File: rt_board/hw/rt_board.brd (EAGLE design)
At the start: 100 x 80 mm, 26 parts, among them IC1 MCP170333MB, Q1 8MHz, U1 STM32F051R8T7, U2 SN74AVC4T245PW, X1 PWR

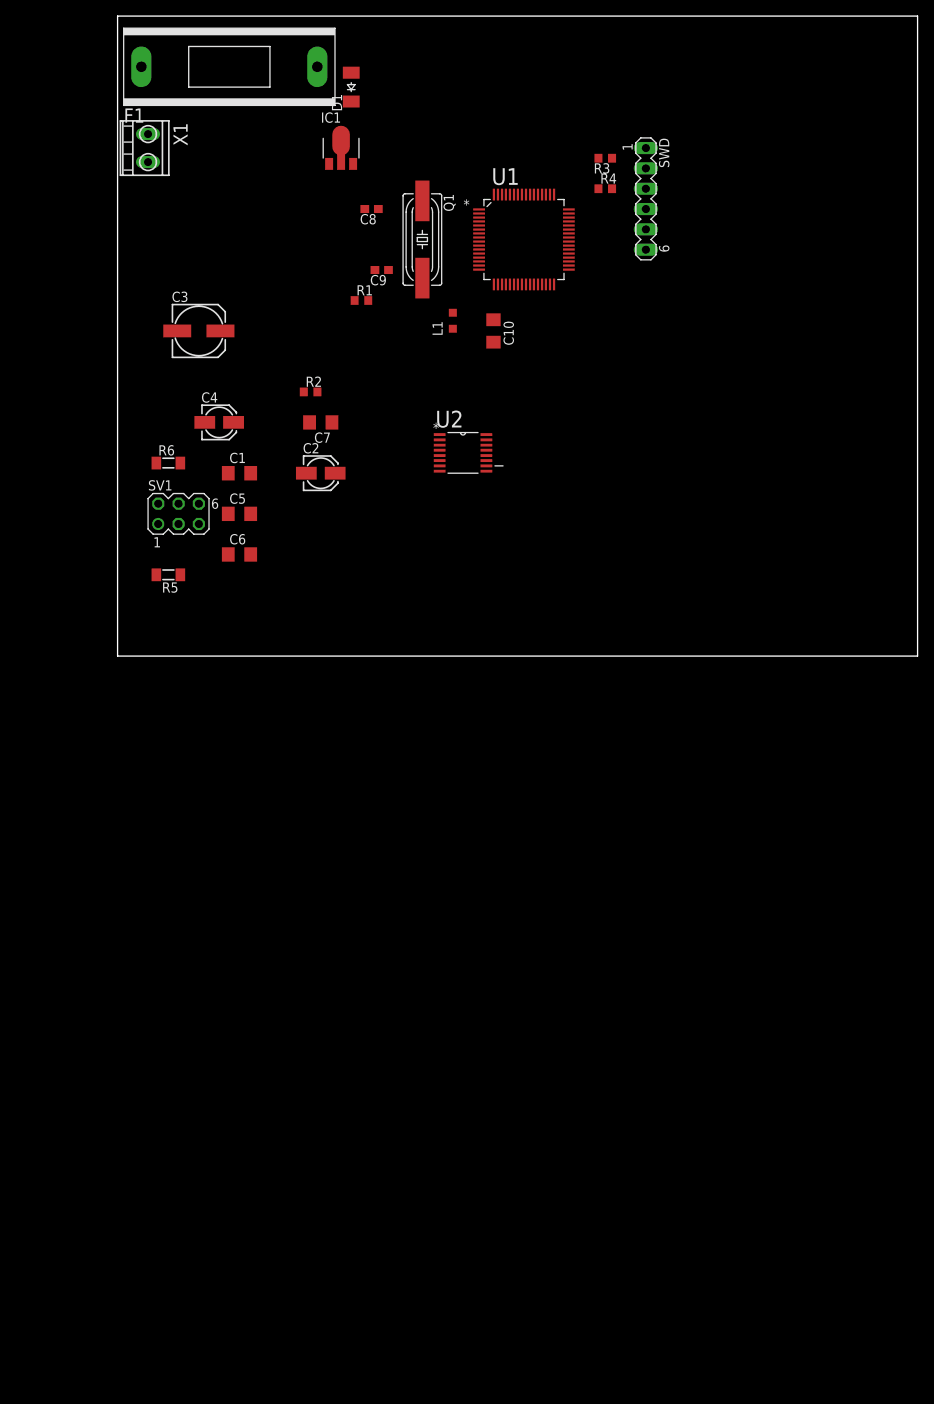
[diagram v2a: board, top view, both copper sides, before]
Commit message: added power outputs and current control circutyr
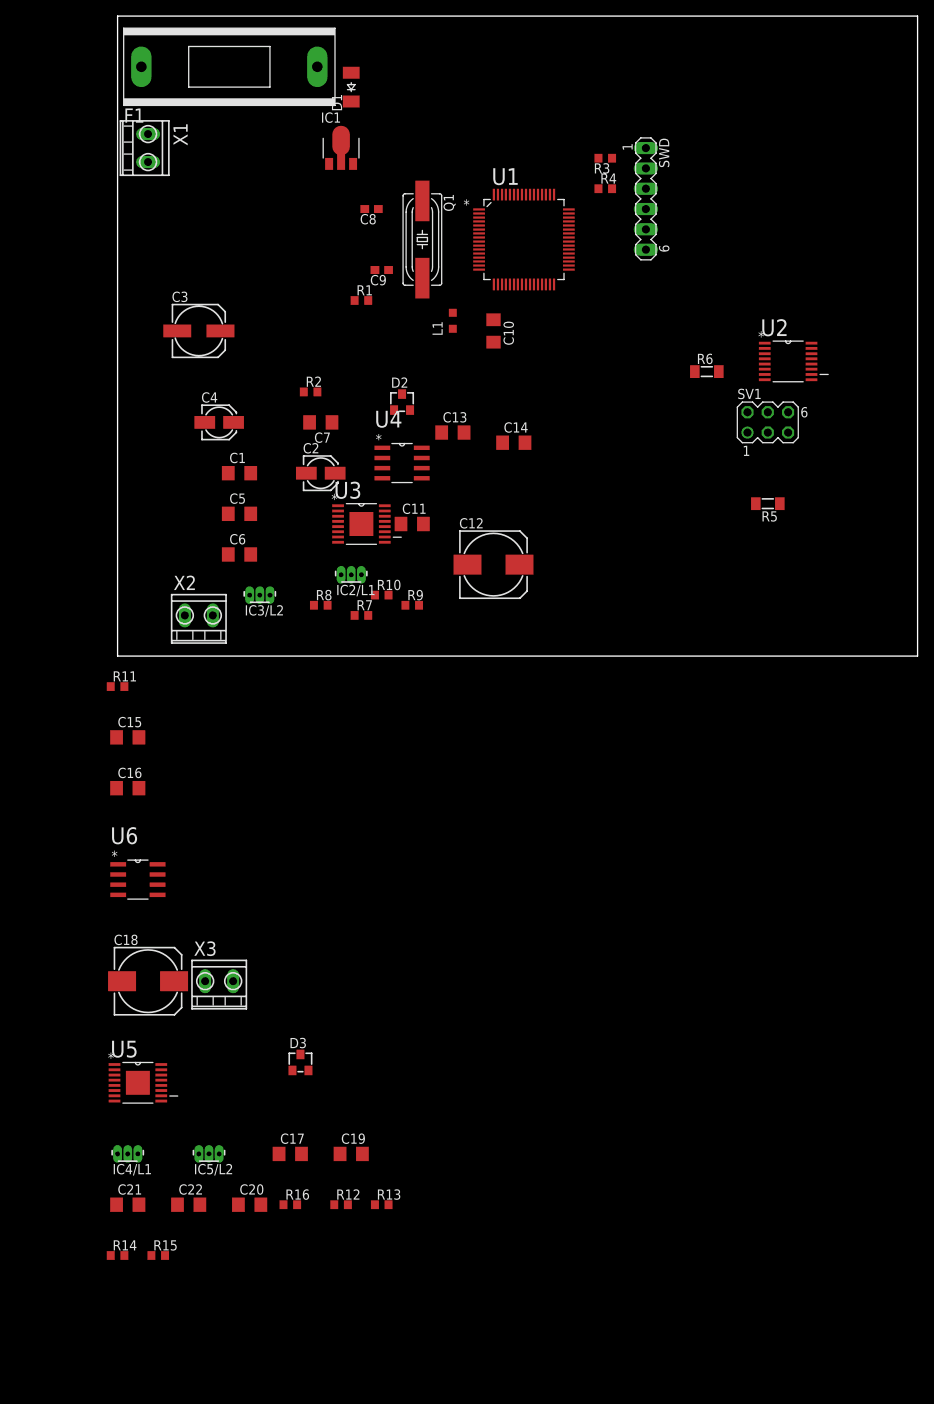
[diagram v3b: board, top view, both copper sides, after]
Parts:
- added C11, C13, C15, C16, C17, C19, C21, C22: 100nF, rcl:C1206
- added C12, C18: 100uF, rcl:153CLV-0810
- added C14, C20: 1nF, rcl:C1206
- added D2, D3: BZX84CSMD, diode:TO236
- added IC2/L1, IC3/L2, IC4/L1, IC5/L2: TLE4935L, allegro:SIP3-UA
- added R10, R13, R15, R8: 3kR, rcl:R0603
- added R11, R16: 3.3kR, rcl:R0603
- added R12, R14, R7, R9: 2kR, rcl:R0603
- added U3, U5: DRV8801PWP, TI-DRV8801PWP:SOP65P640X120-17N
- added U4, U6: ACS712ELCTR-20A-T, Allegro-ACS712ELCTR-20A-T:SOIC127P600X175-8N
- added X2: LEFT, con-ptr500:AK550/2
- added X3: RIGHT, con-ptr500:AK550/2
- moved R5 75.5 mm to (81.3, 19.1)
- moved SV1 74.5 mm to (81.3, 29.2)
- moved R6 68.3 mm to (73.7, 35.6)
- moved U2 42.2 mm to (83.8, 36.8)
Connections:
- new net N$16: IC2/L1.3, R7.1
- new net N$17: R7.2, R8.1, U1.14
- new net N$18: IC3/L2.3, R9.1
- new net N$19: R10.1, R9.2, U1.15
- new net N$20: U3.7, X2.1
- new net N$21: U3.10, X2.2
- new net N$22: U3.8, U4.1, U4.2
- new net N$23: D2.C, U1.20, U4.7
- new net N$24: C14.1, U4.6
- new net N$25: R11.1, U3.5
- new net N$26: C15.2, U3.14
- new net N$27: C16.2, U3.12
- new net N$28: C16.1, U3.11
- new net N$29: IC4/L1.3, R12.1
- new net N$30: R12.2, R13.1, U1.56
- new net N$31: IC5/L2.3, R14.1
- new net N$32: R14.2, R15.1, U1.57
- new net N$33: U5.7, X3.1
- new net N$34: U5.10, X3.2
- new net N$35: C20.1, U6.6
- new net N$36: U5.8, U6.1, U6.2
- new net N$37: D3.C, U1.21, U6.7
- new net N$38: R16.1, U5.5
- new net N$39: C21.2, U5.14
- new net N$40: C22.2, U5.12
- new net N$41: C22.1, U5.11
- new net N$42: U1.34, U3.2, U5.2
- new net N$45: U1.35, U3.6
- new net N$46: U1.36, U5.6
- new net N$48: U1.33, U3.3
- new net N$49: U1.30, U5.3
- net +12V: now also C11.1, C12.+, C15.1, C17.1, C18.+, C21.1, U3.9, U5.9
- net +5V/1: now also C13.1, C19.1, IC2/L1.1, IC3/L2.1, IC4/L1.1, IC5/L2.1, U4.8, U6.8
- net +5V/4: now also R11.2, R16.2
- net 0V: now also C11.2, C12.-, C13.2, C14.2, C17.2, C18.-, C19.2, C20.2, D2.A, D3.A, IC2/L1.2, IC3/L2.2, IC4/L1.2, IC5/L2.2, R10.2, R13.2, R15.2, R8.2, U3.13, U3.16, U3.17, U3.4, U4.3, U4.4, U4.5, U5.13, U5.16, U5.17, U5.4, U6.3, U6.4, U6.5

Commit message: added LED to indicate circut is powered and one user-defined, controlled via uC
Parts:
- added LED1, LED2: GREEN, led:CHIPLED_0603
- added R17: 470R, rcl:R0603
- added U7: 2N7002BKW, 2n7002:SOT65P210X110-3N
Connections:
- new net N$43: LED1.A, R17.2
- new net N$44: U1.26, U7.1
- new net N$47: LED2.C, U7.3
- net +5V: now also LED2.A, R17.1
- net 0V: now also LED1.C, U7.2
- net N$17: now also U1.41; no longer U1.14
- net N$19: now also U1.42; no longer U1.15
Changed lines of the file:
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@@
 <element name="C21" library="rcl" package="C1206" value="100nF" x="1.27" y="-68.58"/>
 <element name="C22" library="rcl" package="C1206" value="100nF" x="8.89" y="-68.58"/>
+<element name="LED1" library="led" package="CHIPLED_0603" value="GREEN" x="-5.08" y="-74.93"/>
+<element name="R17" library="rcl" package="R0603" value="470R" x="-5.08" y="-80.01"/>
+<element name="U7" library="2n7002" package="SOT65P210X110-3N" value="2N7002BKW" x="-2.54" y="-87.63">
+<attribute name="PACKAGE" value="SOT-3" x="-2.54" y="-87.63" size="1.778" layer="27" display="off"/>
+<attribute name="OC_NEWARK" value="55T7739" x="-2.54" y="-87.63" size="1.778" layer="27" display="off"/>
+<attribute name="MPN" value="2N7002BKW" x="-2.54" y="-87.63" size="1.778" layer="27" display="off"/>
+<attribute name="SUPPLIER" value="NXP Semiconductors" x="-2.54" y="-87.63" size="1.778" layer="27" display="off"/>
+<attribute name="OC_FARNELL" value="1894713" x="-2.54" y="-87.63" size="1.778" layer="27" display="off"/>
+</element>
+<element name="LED2" library="led" package="CHIPLED_0603" value="GREEN" x="-10.16" y="-90.17"/>
 </elements>
 <signals>
@@
 <contactref element="U3" pad="16"/>
 <contactref element="U5" pad="16"/>
+<contactref element="LED1" pad="C"/>
+<contactref element="U7" pad="2"/>
 <wire x1="61.81" y1="62.23" x2="66.04" y2="58.42" width="0" layer="19" extent="1-1"/>
 <wire x1="47.5488" y1="57.6834" x2="61.81" y2="62.23" width="0" layer="19" extent="1-1"/>
@@
 <wire x1="33.87" y1="-68.58" x2="30.61" y2="-62.23" width="0" layer="19" extent="1-1"/>
 <wire x1="21.86" y1="-51.8" x2="22.99" y2="-62.23" width="0" layer="19" extent="1-1"/>
-<wire x1="5.93" y1="-74.93" x2="1.27" y2="-62.23" width="0" layer="19" extent="1-1"/>
+<wire x1="-5.08" y1="-74.18" x2="1.27" y2="-62.23" width="0" layer="19" extent="1-1"/>
+<wire x1="5.93" y1="-74.93" x2="-5.08" y2="-74.18" width="0" layer="19" extent="1-1"/>
+<wire x1="-3.4798" y1="-88.2904" x2="-5.08" y2="-74.18" width="0" layer="19" extent="1-1"/>
 </signal>
 <signal name="+5V">
@@
 <contactref element="R4" pad="2"/>
 <contactref element="U2" pad="16"/>
+<contactref element="R17" pad="1"/>
+<contactref element="LED2" pad="A"/>
 <wire x1="61.81" y1="58.42" x2="66.04" y2="63.5" width="0" layer="19" extent="1-1"/>
 <wire x1="54.5592" y1="46.4566" x2="61.81" y2="58.42" width="0" layer="19" extent="1-1"/>
@@
 <wire x1="41.91" y1="40.91" x2="54.5592" y2="46.4566" width="0" layer="19" extent="1-1"/>
 <wire x1="29.439" y1="61.519" x2="45.1866" y2="55.8292" width="0" layer="19" extent="1-1"/>
-<wire x1="86.741" y1="39.116" x2="41.91" y2="40.91" width="0" layer="19" extent="1-1"/>
 <wire x1="23.28" y1="33.02" x2="41.91" y2="40.91" width="0" layer="19" extent="1-1"/>
 <wire x1="14.5" y1="29.21" x2="23.28" y2="33.02" width="0" layer="19" extent="1-1"/>
@@
 <wire x1="13.84" y1="12.7" x2="13.84" y2="17.78" width="0" layer="19" extent="1-1"/>
 <wire x1="27.2" y1="22.86" x2="23.28" y2="33.02" width="0" layer="19" extent="1-1"/>
+<wire x1="86.741" y1="39.116" x2="61.81" y2="58.42" width="0" layer="19" extent="1-1"/>
+<wire x1="-5.93" y1="-80.01" x2="13.84" y2="12.7" width="0" layer="19" extent="1-1"/>
+<wire x1="-10.16" y1="-90.92" x2="-5.93" y2="-80.01" width="0" layer="19" extent="1-1"/>
 </signal>
 <signal name="+12V">
@@
 <contactref element="R7" pad="2"/>
 <contactref element="R8" pad="1"/>
-<contactref element="U1" pad="14"/>
-<wire x1="31.33" y1="5.08" x2="45.1866" y2="49.3268" width="0" layer="19" extent="1-1"/>
+<contactref element="U1" pad="41"/>
+<wire x1="31.33" y1="5.08" x2="56.4134" y2="52.324" width="0" layer="19" extent="1-1"/>
 <wire x1="24.55" y1="6.35" x2="31.33" y2="5.08" width="0" layer="19" extent="1-1"/>
 </signal>
@@
 <contactref element="R9" pad="2"/>
 <contactref element="R10" pad="1"/>
-<contactref element="U1" pad="15"/>
-<wire x1="37.68" y1="6.35" x2="45.1866" y2="48.8188" width="0" layer="19" extent="1-1"/>
+<contactref element="U1" pad="42"/>
+<wire x1="37.68" y1="6.35" x2="56.4134" y2="52.832" width="0" layer="19" extent="1-1"/>
 <wire x1="32.17" y1="7.62" x2="37.68" y2="6.35" width="0" layer="19" extent="1-1"/>
 </signal>
@@
 <wire x1="-0.381" y1="-52.3748" x2="53.5432" y2="46.4566" width="0" layer="19" extent="1-1"/>
 </signal>
+<signal name="N$43">
+<contactref element="LED1" pad="A"/>
+<contactref element="R17" pad="2"/>
+<wire x1="-5.08" y1="-75.68" x2="-4.23" y2="-80.01" width="0" layer="19" extent="1-1"/>
+</signal>
+<signal name="N$44">
+<contactref element="U1" pad="26"/>
+<contactref element="U7" pad="1"/>
+<wire x1="-3.4798" y1="-86.9696" x2="51.562" y2="46.4566" width="0" layer="19" extent="1-1"/>
+</signal>
+<signal name="N$47">
+<contactref element="U7" pad="3"/>
+<contactref element="LED2" pad="C"/>
+<wire x1="-1.6002" y1="-87.63" x2="-10.16" y2="-89.42" width="0" layer="19" extent="1-1"/>
+</signal>
 </signals>

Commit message: added boot0 and reset switches
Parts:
- added SW1, SW2: B3U-1000PM-B, basz:SPST-NO
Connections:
- net +5V: now also SW1.P$2
- net 0V: now also SW2.P$1
- net N$5: now also SW1.P$1
- net N$6: now also SW2.P$2
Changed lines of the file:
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@@
 </element>
 <element name="LED2" library="led" package="CHIPLED_0603" value="GREEN" x="-10.16" y="-90.17"/>
+<element name="SW1" library="basz" package="SPST-NO" value="B3U-1000PM-B" x="60.96" y="12.7"/>
+<element name="SW2" library="basz" package="SPST-NO" value="B3U-1000PM-B" x="67.31" y="7.62"/>
 </elements>
 <signals>
@@
 <contactref element="LED1" pad="C"/>
 <contactref element="U7" pad="2"/>
+<contactref element="SW2" pad="P$1"/>
 <wire x1="61.81" y1="62.23" x2="66.04" y2="58.42" width="0" layer="19" extent="1-1"/>
 <wire x1="47.5488" y1="57.6834" x2="61.81" y2="62.23" width="0" layer="19" extent="1-1"/>
@@
 <wire x1="5.93" y1="-74.93" x2="-5.08" y2="-74.18" width="0" layer="19" extent="1-1"/>
 <wire x1="-3.4798" y1="-88.2904" x2="-5.08" y2="-74.18" width="0" layer="19" extent="1-1"/>
+<wire x1="65.81" y1="7.62" x2="-3.4798" y2="-88.2904" width="0" layer="19" extent="1-1"/>
 </signal>
 <signal name="+5V">
@@
 <contactref element="R17" pad="1"/>
 <contactref element="LED2" pad="A"/>
+<contactref element="SW1" pad="P$2"/>
 <wire x1="61.81" y1="58.42" x2="66.04" y2="63.5" width="0" layer="19" extent="1-1"/>
 <wire x1="54.5592" y1="46.4566" x2="61.81" y2="58.42" width="0" layer="19" extent="1-1"/>
@@
 <wire x1="-5.93" y1="-80.01" x2="13.84" y2="12.7" width="0" layer="19" extent="1-1"/>
 <wire x1="-10.16" y1="-90.92" x2="-5.93" y2="-80.01" width="0" layer="19" extent="1-1"/>
+<wire x1="62.46" y1="12.7" x2="-10.16" y2="-90.92" width="0" layer="19" extent="1-1"/>
 </signal>
 <signal name="+12V">
@@
 <contactref element="U1" pad="60"/>
 <contactref element="R1" pad="2"/>
+<contactref element="SW1" pad="P$1"/>
 <wire x1="31.33" y1="44.45" x2="49.0474" y2="57.6834" width="0" layer="19" extent="1-1"/>
+<wire x1="59.46" y1="12.7" x2="31.33" y2="44.45" width="0" layer="19" extent="1-1"/>
 </signal>
 <signal name="N$6">
@@
 <contactref element="C7" pad="1"/>
 <contactref element="SWD" pad="5"/>
+<contactref element="SW2" pad="P$2"/>
 <wire x1="45.1866" y1="52.832" x2="66.04" y2="53.34" width="0" layer="19" extent="1-1"/>
 <wire x1="24.98" y1="33.02" x2="45.1866" y2="52.832" width="0" layer="19" extent="1-1"/>
 <wire x1="26.8" y1="29.21" x2="24.98" y2="33.02" width="0" layer="19" extent="1-1"/>
+<wire x1="68.81" y1="7.62" x2="26.8" y2="29.21" width="0" layer="19" extent="1-1"/>
 </signal>
 <signal name="N$7">

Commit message: changed quartz package
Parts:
- Q1: device crystal:SM49 -> crystal:MC-405
- moved Q1 1.27 mm to (39.4, 52.1)
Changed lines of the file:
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@@
 <element name="R2" library="rcl" package="R0603" value="1kR" x="24.13" y="33.02"/>
 <element name="C7" library="rcl" package="C1206" value="100nF" x="25.4" y="29.21" rot="R180"/>
-<element name="Q1" library="crystal" package="SM49" value="8MHz" x="38.1" y="52.07" rot="R270">
-<attribute name="OC_NEWARK" value="unknown" x="38.1" y="52.07" size="1.778" layer="27" rot="R270" display="off"/>
-<attribute name="MPN" value="" x="38.1" y="52.07" size="1.778" layer="27" rot="R270" display="off"/>
-<attribute name="MF" value="" x="38.1" y="52.07" size="1.778" layer="27" rot="R270" display="off"/>
-<attribute name="OC_FARNELL" value="unknown" x="38.1" y="52.07" size="1.778" layer="27" rot="R270" display="off"/>
+<element name="Q1" library="crystal" package="MC-405" value="8MHz" x="39.37" y="52.07" rot="R270">
+<attribute name="OC_NEWARK" value="unknown" x="39.37" y="52.07" size="1.778" layer="27" rot="R270" display="off"/>
+<attribute name="MPN" value="" x="39.37" y="52.07" size="1.778" layer="27" rot="R270" display="off"/>
+<attribute name="MF" value="" x="39.37" y="52.07" size="1.778" layer="27" rot="R270" display="off"/>
+<attribute name="OC_FARNELL" value="unknown" x="39.37" y="52.07" size="1.778" layer="27" rot="R270" display="off"/>
 </element>
 <element name="C8" library="rcl" package="C0603" value="20pF" x="31.75" y="55.88" rot="R180"/>
@@
 <contactref element="C8" pad="1"/>
 <contactref element="U1" pad="5"/>
-<wire x1="38.1" y1="56.896" x2="45.1866" y2="53.8226" width="0" layer="19" extent="1-1"/>
-<wire x1="32.6" y1="55.88" x2="38.1" y2="56.896" width="0" layer="19" extent="1-1"/>
+<wire x1="39.37" y1="56.07" x2="45.1866" y2="53.8226" width="0" layer="19" extent="1-1"/>
+<wire x1="32.6" y1="55.88" x2="39.37" y2="56.07" width="0" layer="19" extent="1-1"/>
 </signal>
 <signal name="N$8">
@@
 <contactref element="C9" pad="1"/>
 <contactref element="U1" pad="6"/>
-<wire x1="38.1" y1="47.244" x2="45.1866" y2="53.3146" width="0" layer="19" extent="1-1"/>
-<wire x1="33.87" y1="48.26" x2="38.1" y2="47.244" width="0" layer="19" extent="1-1"/>
+<wire x1="39.37" y1="48.07" x2="45.1866" y2="53.3146" width="0" layer="19" extent="1-1"/>
+<wire x1="33.87" y1="48.26" x2="39.37" y2="48.07" width="0" layer="19" extent="1-1"/>
 </signal>
 <signal name="N$3">

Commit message: replaced ACS712ELCTR-20A-T with more acurate in a given range ACS712ELCTR-05B-T
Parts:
- U4, U6: value ACS712ELCTR-20A-T -> ACS712ELCTR-05B-T
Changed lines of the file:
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@@
 <element name="C11" library="rcl" package="C1206" value="100nF" x="36.83" y="16.51"/>
 <element name="C12" library="rcl" package="153CLV-0810" value="100uF" x="46.99" y="11.43"/>
-<element name="U4" library="Allegro-ACS712ELCTR-20A-T" package="SOIC127P600X175-8N" value="ACS712ELCTR-20A-T" x="35.56" y="24.13">
+<element name="U4" library="Allegro-ACS712ELCTR-20A-T" package="SOIC127P600X175-8N" value="ACS712ELCTR-05B-T" x="35.56" y="24.13">
 <attribute name="PACKAGE" value="SOIC-8" x="35.56" y="24.13" size="1.778" layer="27" display="off"/>
 <attribute name="OC_NEWARK" value="31M3133" x="35.56" y="24.13" size="1.778" layer="27" display="off"/>
@@
 <element name="C17" library="rcl" package="C1206" value="100nF" x="21.59" y="-62.23"/>
 <element name="C18" library="rcl" package="153CLV-0810" value="100uF" x="3.81" y="-40.64"/>
-<element name="U6" library="Allegro-ACS712ELCTR-20A-T" package="SOIC127P600X175-8N" value="ACS712ELCTR-20A-T" x="2.54" y="-27.94">
+<element name="U6" library="Allegro-ACS712ELCTR-20A-T" package="SOIC127P600X175-8N" value="ACS712ELCTR-05B-T" x="2.54" y="-27.94">
 <attribute name="PACKAGE" value="SOIC-8" x="-33.02" y="-66.04" size="1.778" layer="27" display="off"/>
 <attribute name="OC_NEWARK" value="31M3133" x="-33.02" y="-66.04" size="1.778" layer="27" display="off"/>
